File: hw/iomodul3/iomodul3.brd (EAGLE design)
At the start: 65 x 48 mm, 61 parts, among them CN2 PINHEAD-2x5-P1.27, IC1 MCP2551, IC2 SAMD21G18A-AUT, IC4 MCP1700T3302E/TT, IC5 DS8289, Y1 32,768Khz_SMD, Y4 32,768Khz_SMD

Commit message: mod of CANable USB to CAN modul
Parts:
- removed C23, C24: 22p, schlager_passiv:C0805
- removed Y4: 32,768Khz_SMD, Cristalli:RESONATOR_EPSON_FC_145
- moved C21 4.59 mm to (22.2, 24.9), flipped to the bottom, turned to 0 degrees
- moved C20 4.04 mm to (27.5, 24.9), flipped to the bottom, turned to 180 degrees
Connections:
- removed net FGND: CON2.T1, CON2.T2
- removed net LED3_: R12.2, R13.2
- removed net LED4_: R11.2, R14.2
- removed net PA14_TCC0-W4: IC2.23
- removed net PA15_TCC0-W5: IC2.24
- new net #5_LED1: IC2.24, R12.2, R13.2
- new net #6_LED2: IC2.23, R11.2, R14.2
- net GND: no longer C23.1, C24.1
- net PA00_XIN32: no longer C23.2, Y4.P$2
- net PA01_XOUT32: no longer C24.2, Y4.P$1
- net PE: now also CON2.T1, CON2.T2
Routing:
- net #6_LED2: track 0.00 -> 43.2 mm, vias 0 -> 4
- net #5_LED1: track 0.00 -> 42.3 mm, vias 0 -> 3
- net PE: track 15.5 -> 31.0 mm
- net FGND: track 15.5 -> 0.00 mm
- net GND: track 17.8 -> 12.3 mm, vias 11 -> 30
- net PA01_XOUT32: track 5.81 -> 3.10 mm
- net PA00_XIN32: track 7.43 -> 4.94 mm
- net +3V3: track 112.8 -> 111.5 mm, vias 5 -> 4
- net VDDCORE: track 2.64 -> 3.16 mm, vias 0 -> 1

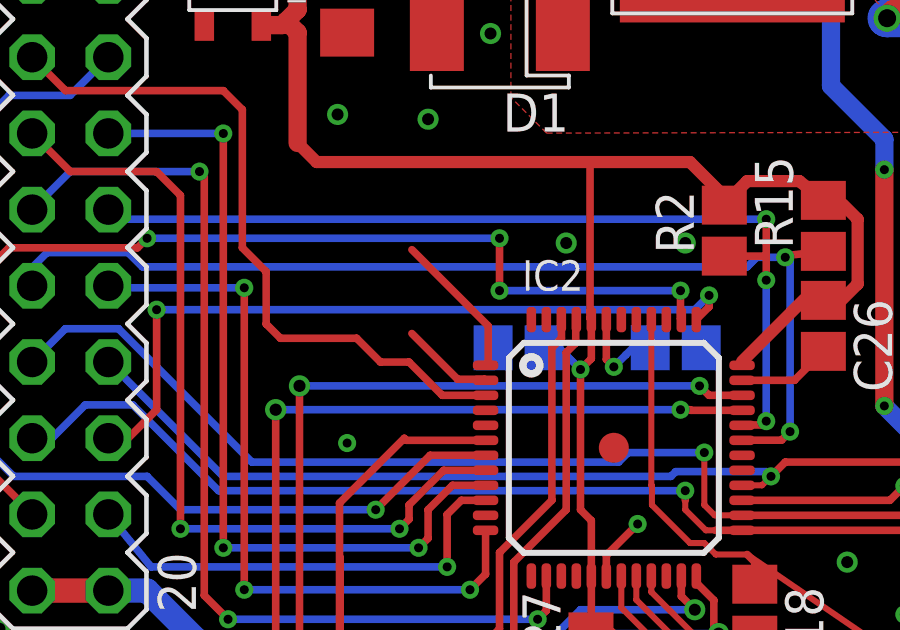
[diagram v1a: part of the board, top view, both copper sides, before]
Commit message: added readme and cleanup
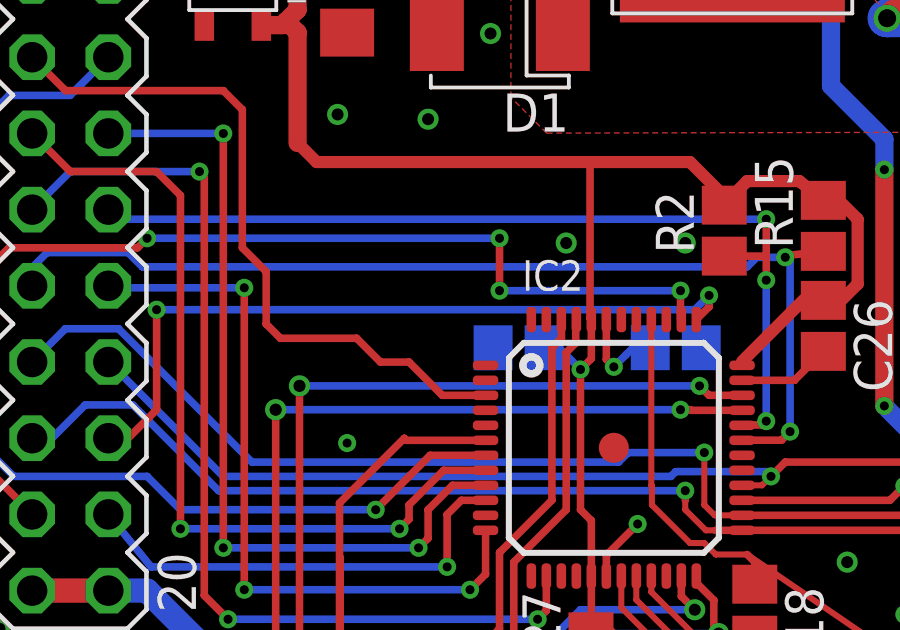
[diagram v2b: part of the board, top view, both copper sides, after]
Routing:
- net PA00_XIN32: track 4.94 -> 0.00 mm
- net PA01_XOUT32: track 3.10 -> 0.00 mm
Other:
- board text removed: "C1"
- board text removed: "C10"
- board text removed: "C11"
- board text removed: "C12"
- board text removed: "C13"
- board text removed: "C14"
- board text removed: "C15"
- board text removed: "C16"
- board text removed: "C2"
- board text removed: "C25"
- board text removed: "C3"
- board text removed: "C4"
- board text removed: "C5"
- board text removed: "C6"
- board text removed: "C7"
- board text removed: "C8"
- board text removed: "C9"
- board text removed: "CON1"
- board text removed: "CON2"
- board text removed: "D1"
- board text removed: "D2"
- board text removed: "IC1"
- board text removed: "IC3"
- board text removed: "IC4"
- board text removed: "IC5"
- board text removed: "JP1"
- board text removed: "JP2"
- board text removed: "L3"
- board text removed: "LED1"
- board text removed: "LED2"
- board text removed: "Q2"
- board text removed: "R1"
- board text removed: "R10"
- board text removed: "R2"
- board text removed: "R3"
- board text removed: "R4"
- board text removed: "R5"
- board text removed: "R6"
- board text removed: "R7"
- board text removed: "R8"
- board text removed: "R9"
- board text removed: "SV1"
- board text removed: "SWD"
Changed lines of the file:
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@@
 <layer number="24" name="bOrigins" color="15" fill="1" visible="yes" active="yes"/>
 <layer number="25" name="tNames" color="7" fill="1" visible="yes" active="yes"/>
-<layer number="26" name="bNames" color="7" fill="1" visible="no" active="yes"/>
-<layer number="27" name="tValues" color="7" fill="1" visible="no" active="yes"/>
-<layer number="28" name="bValues" color="7" fill="1" visible="no" active="yes"/>
-<layer number="29" name="tStop" color="7" fill="3" visible="no" active="yes"/>
-<layer number="30" name="bStop" color="7" fill="6" visible="no" active="yes"/>
-<layer number="31" name="tCream" color="7" fill="4" visible="no" active="yes"/>
-<layer number="32" name="bCream" color="7" fill="5" visible="no" active="yes"/>
-<layer number="33" name="tFinish" color="6" fill="3" visible="no" active="yes"/>
-<layer number="34" name="bFinish" color="6" fill="6" visible="no" active="yes"/>
-<layer number="35" name="tGlue" color="7" fill="4" visible="no" active="yes"/>
-<layer number="36" name="bGlue" color="7" fill="5" visible="no" active="yes"/>
-<layer number="37" name="tTest" color="7" fill="1" visible="no" active="yes"/>
-<layer number="38" name="bTest" color="7" fill="1" visible="no" active="yes"/>
-<layer number="39" name="tKeepout" color="4" fill="11" visible="no" active="yes"/>
-<layer number="40" name="bKeepout" color="1" fill="11" visible="no" active="yes"/>
-<layer number="41" name="tRestrict" color="4" fill="10" visible="no" active="yes"/>
-<layer number="42" name="bRestrict" color="1" fill="10" visible="no" active="yes"/>
-<layer number="43" name="vRestrict" color="2" fill="10" visible="no" active="yes"/>
-<layer number="44" name="Drills" color="7" fill="1" visible="no" active="yes"/>
-<layer number="45" name="Holes" color="7" fill="1" visible="no" active="yes"/>
-<layer number="46" name="Milling" color="3" fill="1" visible="no" active="yes"/>
-<layer number="47" name="Measures" color="7" fill="1" visible="no" active="yes"/>
-<layer number="48" name="Document" color="7" fill="1" visible="no" active="yes"/>
+<layer number="26" name="bNames" color="7" fill="1" visible="yes" active="yes"/>
+<layer number="27" name="tValues" color="7" fill="1" visible="yes" active="yes"/>
+<layer number="28" name="bValues" color="7" fill="1" visible="yes" active="yes"/>
+<layer number="29" name="tStop" color="7" fill="3" visible="yes" active="yes"/>
+<layer number="30" name="bStop" color="7" fill="6" visible="yes" active="yes"/>
+<layer number="31" name="tCream" color="7" fill="4" visible="yes" active="yes"/>
+<layer number="32" name="bCream" color="7" fill="5" visible="yes" active="yes"/>
+<layer number="33" name="tFinish" color="6" fill="3" visible="yes" active="yes"/>
+<layer number="34" name="bFinish" color="6" fill="6" visible="yes" active="yes"/>
+<layer number="35" name="tGlue" color="7" fill="4" visible="yes" active="yes"/>
+<layer number="36" name="bGlue" color="7" fill="5" visible="yes" active="yes"/>
+<layer number="37" name="tTest" color="7" fill="1" visible="yes" active="yes"/>
+<layer number="38" name="bTest" color="7" fill="1" visible="yes" active="yes"/>
+<layer number="39" name="tKeepout" color="4" fill="11" visible="yes" active="yes"/>
+<layer number="40" name="bKeepout" color="1" fill="11" visible="yes" active="yes"/>
+<layer number="41" name="tRestrict" color="4" fill="10" visible="yes" active="yes"/>
+<layer number="42" name="bRestrict" color="1" fill="10" visible="yes" active="yes"/>
+<layer number="43" name="vRestrict" color="2" fill="10" visible="yes" active="yes"/>
+<layer number="44" name="Drills" color="7" fill="1" visible="yes" active="yes"/>
+<layer number="45" name="Holes" color="7" fill="1" visible="yes" active="yes"/>
+<layer number="46" name="Milling" color="3" fill="1" visible="yes" active="yes"/>
+<layer number="47" name="Measures" color="7" fill="1" visible="yes" active="yes"/>
+<layer number="48" name="Document" color="7" fill="1" visible="yes" active="yes"/>
 <layer number="49" name="Reference" color="7" fill="1" visible="yes" active="yes"/>
 <layer number="50" name="dxf" color="7" fill="1" visible="no" active="no"/>
@@
 <text x="59.660003125" y="31.25" size="1.27" layer="126" rot="MR90">BR1</text>
 <text x="55.760009375" y="16.21" size="1.27" layer="126" rot="MR270">BR2</text>
-<text x="35.76" y="11.18199375" size="0.799996875" layer="125" ratio="15">C1</text>
-<text x="15.89999375" y="26.72999375" size="0.799996875" layer="125" ratio="15" rot="R270">C2</text>
-<text x="29.3600125" y="11.662003125" size="0.799996875" layer="125" ratio="15" rot="R90">C3</text>
-<text x="35.889996875" y="5.80750625" size="0.799996875" layer="125" ratio="15" rot="R270">C4</text>
-<text x="31.80999375" y="15.920009375" size="0.799996875" layer="125" ratio="15" rot="R180">C5</text>
-<text x="34.470009375" y="21.63000625" size="0.799996875" layer="125" ratio="15" rot="R180">C6</text>
-<text x="18.4999875" y="29.090009375" size="0.799996875" layer="125" ratio="15" rot="R270">C7</text>
-<text x="51.950009375" y="44.330009375" size="0.799996875" layer="125" ratio="15" rot="R180">C8</text>
-<text x="27.820009375" y="11.872009375" size="0.799996875" layer="125" ratio="15" rot="R90">C9</text>
-<text x="32.66000625" y="24.249990625" size="0.799996875" layer="125" ratio="15" rot="R180">C10</text>
-<text x="35.070009375" y="19.830009375" size="0.799996875" layer="125" ratio="15">C11</text>
-<text x="51.940003125" y="3.76999375" size="0.799996875" layer="125" ratio="15" rot="R180">C12</text>
-<text x="39.4200125" y="32.3699875" size="0.799996875" layer="125" ratio="15" rot="R180">C13</text>
-<text x="15.82300625" y="44.109996875" size="1.27" layer="125">C14</text>
-<text x="20.312990625" y="44.09000625" size="1.27" layer="125">C15</text>
-<text x="15.04" y="36.500003125" size="0.799996875" layer="125" ratio="15">C16</text>
-<text x="42.639996875" y="32.4429875" size="1.27" layer="125" rot="R90">C25</text>
-<text x="48.3100125" y="26.499996875" size="1.27" layer="125" rot="R90">CON1</text>
-<text x="48.430003125" y="5.260009375" size="1.27" layer="125" rot="R90">CON2</text>
-<text x="23.900003125" y="33.400009375" size="1.27" layer="125" rot="R180">D1</text>
-<text x="44.2729875" y="40.621990625" size="1.27" layer="125" ratio="10">D2</text>
-<text x="39.205003125" y="16.8140125" size="1.27" layer="125">IC1</text>
-<text x="22.940009375" y="14.92999375" size="1.27" layer="125" rot="R180">IC3</text>
-<text x="12.0800125" y="36.589996875" size="0.6096" layer="121">IC4</text>
-<text x="40.980003125" y="34.04600625" size="1.016" layer="125" rot="R180">IC5</text>
-<text x="40.313990625" y="27.66100625" size="1.27" layer="125" ratio="10">JP1</text>
-<text x="42.893996875" y="30.320996875" size="1.27" layer="125" ratio="10">JP2</text>
-<text x="28.110003125" y="45.030009375" size="1.27" layer="125">L3</text>
-<text x="63.740003125" y="25.7849875" size="1.27" layer="125" rot="R90">LED1</text>
-<text x="63.97500625" y="16.829990625" size="1.27" layer="125" rot="R90">LED2</text>
-<text x="37.0800125" y="18.08" size="1.016" layer="125" rot="R180">Q2</text>
-<text x="47.695003125" y="18.5999875" size="1.27" layer="125" rot="R180">R1</text>
-<text x="23.724996875" y="10.73500625" size="1.27" layer="125">R2</text>
-<text x="-26.035" y="30.625009375" size="1.27" layer="125" rot="R180">R3</text>
-<text x="37.48999375" y="5.767503125" size="0.799996875" layer="125" ratio="15" rot="R270">R4</text>
-<text x="-23.349990625" y="33.96500625" size="1.27" layer="125" rot="R180">R5</text>
-<text x="33.53000625" y="24.770003125" size="0.799996875" layer="125" ratio="15">R6</text>
-<text x="40.250009375" y="43.099990625" size="0.799996875" layer="125" ratio="15" rot="R180">R7</text>
-<text x="38.370003125" y="38.2500125" size="0.799996875" layer="125" ratio="15">R8</text>
-<text x="51.940003125" y="46.260003125" size="0.799996875" layer="125" ratio="15" rot="R180">R9</text>
-<text x="51.940003125" y="1.950009375" size="0.799996875" layer="125" ratio="15" rot="R180">R10</text>
-<text x="10.200996875" y="40.959990625" size="1.27" layer="125" ratio="10" rot="R270">SV1</text>
-<text x="10.95499375" y="12.100990625" size="1.27" layer="125" ratio="10">SWD</text>
 <text x="12.17" y="1" size="1.016" layer="1">CAN-IOModul, 06'15 artwork by
 Sarah, Fablab KA
@@
 <signal name="PA00_XIN32">
 <contactref element="IC2" pad="1"/>
-<wire x1="18.669" y1="28.194" x2="21.209" y2="25.654" width="0.254" layer="1"/>
-<wire x1="21.209" y1="25.654" x2="21.209" y2="24.424" width="0.254" layer="1"/>
-<wire x1="21.209" y1="24.424" x2="21.125" y2="24.34" width="0.254" layer="1"/>
 </signal>
 <signal name="PA01_XOUT32">
 <contactref element="IC2" pad="2"/>
-<wire x1="18.669" y1="25.4" x2="20.193" y2="23.876" width="0.254" layer="1"/>
-<wire x1="20.193" y1="23.876" x2="21.089" y2="23.876" width="0.254" layer="1"/>
-<wire x1="21.089" y1="23.876" x2="21.125" y2="23.84" width="0.254" layer="1"/>
 </signal>
 <signal name="DGI_GPIO0">
